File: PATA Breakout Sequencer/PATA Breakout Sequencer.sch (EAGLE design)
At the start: 11 parts

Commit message: some board layout
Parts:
- removed V10, V9: 74595N, 74ttl-din:74595N
- added IC1, IC2, IC3, IC4, IC5: 74HC165N, 74xx-eu:74HC165N
- added R1, R10, R11, R12, R13, R14, R15, R16, R17, R18, R19, R2, R20, R21, R22, R23, R24, R25, R26, R27, R28, R29, R3, R30, R31, R32, R33, R34, R35, R36, R37, R38, R39, R4, R40, R5, R6, R7, R8, R9: (no value), rcl:R-US_0204/5
- added SV2: (no value), con-lsta:FE20-2
- added SV3: (no value), con-lsta:FE15-2
- added SV5: (no value), con-lsta:FE18-2
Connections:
- new net A0: IC1A.A, R8.1, SV3.1, SV3.30
- new net A1: IC2A.A, R16.1
- new net A10: V61.QA
- new net A11: V71.QA
- new net A12: V81.QA
- new net A2: IC3A.A, R24.1
- new net A3: IC4A.A, R32.1
- new net A4: IC5A.A, R40.1
- new net A5: V11.QA
- new net A6: V21.QA
- new net A7: V31.QA
- new net A8: V41.QA
- new net A9: V51.QA
- new net B0: IC1A.B, R7.1, SV3.3
- new net B1: IC2A.B, R15.1
- new net B10: V61.QB
- new net B11: V71.QB
- new net B12: V81.QB
- new net B2: IC3A.B, R23.1
- new net B3: IC4A.B, R31.1
- new net B4: IC5A.B, R39.1
- new net B5: V11.QB
- new net B6: V21.QB
- new net B7: V31.QB
- new net B8: V41.QB
- new net B9: V51.QB
- new net C0: IC1A.C, R6.1, SV3.5
- new net C1: IC2A.C, R14.1
- new net C10: V61.QC
- new net C11: V71.QC
- new net C12: V81.QC
- new net C2: IC3A.C, R22.1
- new net C3: IC4A.C, R30.1
- new net C4: IC5A.C, R38.1
- new net C5: V11.QC
- new net C6: V21.QC
- new net C7: V31.QC
- new net C8: V41.QC
- new net C9: V51.QC
- new net D0: IC1A.D, R5.1, SV3.7
- new net D1: IC2A.D, R13.1
- new net D10: V61.QD
- new net D11: V71.QD
- new net D12: V81.QD
- new net D2: IC3A.D, R21.1
- new net D3: IC4A.D, R29.1
- new net D4: IC5A.D, R37.1
- new net D5: V11.QD
- new net D6: V21.QD
- new net D7: V31.QD
- new net D8: V41.QD
- new net D9: V51.QD
- new net E0: IC1A.E, R4.1, SV3.9
- new net E1: IC2A.E, R12.1
- new net E10: V61.QE
- new net E11: V71.QE
- new net E12: V81.QE
- new net E2: IC3A.E, R20.1
- new net E3: IC4A.E, R28.1
- new net E4: IC5A.E, R36.1
- new net E5: V11.QE
- new net E6: V21.QE
- new net E7: V31.QE
- new net E8: V41.QE
- new net E9: V51.QE
- new net F0: IC1A.F, R3.1, SV3.11
- new net F1: IC2A.F, R11.1
- new net F10: V61.QF
- new net F11: V71.QF
- new net F12: V81.QF
- new net F2: IC3A.F, R19.1
- new net F3: IC4A.F, R27.1
- new net F4: IC5A.F, R35.1
- new net F5: V11.QF
- new net F6: V21.QF
- new net F7: V31.QF
- new net F8: V41.QF
- new net F9: V51.QF
- new net G0: IC1A.G, R2.1, SV3.13
- new net G1: IC2A.G, R10.1
- new net G10: V61.QG
- new net G11: V71.QG
- new net G12: V81.QG
- new net G2: IC3A.G, R18.1
- new net G3: IC4A.G, R26.1
- new net G4: IC5A.G, R34.1
- new net G5: V11.QG
- new net G6: V21.QG
- new net G7: V31.QG
- new net G8: V41.QG
- new net G9: V51.QG
- new net H0: IC1A.H, R1.1, SV3.15
- new net H1: IC2A.H, R9.1
- new net H10: V61.QH
- new net H11: V71.QH
- new net H12: V81.QH
- new net H2: IC3A.H, R17.1
- new net H3: IC4A.H, R25.1
- new net H4: IC5A.H, R33.1
- new net H5: V11.QH
- new net H6: V21.QH
- new net H7: V31.QH
- new net H8: V41.QH
- new net H9: V51.QH
- new net N$10: SV3.16
- new net N$11: SV3.14
- new net N$12: SV3.12
- new net N$13: SV3.10
- new net N$14: SV3.8
- new net N$15: SV3.6
- new net N$16: SV3.4
- new net N$17: SV3.2
- new net N$21: SV3.29
- new net N$22: SV3.27
- new net N$23: SV3.25
- new net N$24: SV3.23
- new net N$25: SV3.21
- new net N$26: SV3.19
- new net N$27: SV3.17
- new net N$4: SV3.28
- new net N$5: SV3.26
- new net N$6: SV3.24
- new net N$7: SV3.22
- new net N$8: SV3.20
- new net N$9: SV3.18
- new net OUT0: V11.QH*, V21.SER
- new net OUT1: IC1A.SER, IC2A.QH, V21.QH*, V31.SER
- new net OUT2: IC2A.SER, IC3A.QH, V31.QH*, V41.SER
- new net OUT3: IC3A.SER, IC4A.QH, V41.QH*, V51.SER
- new net OUT4: IC4A.SER, IC5A.QH, V51.QH*, V61.SER
- new net OUT5: V61.QH*, V71.SER
- new net OUT6: V71.QH*, V81.SER
- new net OUT7: V81.QH*
- net +5V: now also R1.2, R10.2, R11.2, R12.2, R13.2, R14.2, R15.2, R16.2, R17.2, R18.2, R19.2, R2.2, R20.2, R21.2, R22.2, R23.2, R24.2, R25.2, R26.2, R27.2, R28.2, R29.2, R3.2, R30.2, R31.2, R32.2, R33.2, R34.2, R35.2, R36.2, R37.2, R38.2, R39.2, R4.2, R40.2, R5.2, R6.2, R7.2, R8.2, R9.2
- net DGND: now also IC1A.INH, IC2A.INH, IC3A.INH, IC4A.INH, IC5A.INH, IC5A.SER, V11.!G, V21.!G, V31.!G, V41.!G, V51.!G, V61.!G, V71.!G, V81.!G
- net LATCH_IN: now also IC1A.SH/!LD, IC2A.SH/!LD, IC3A.SH/!LD, IC4A.SH/!LD, IC5A.SH/!LD
- net LATCH_OUT: now also V11.RCK, V21.RCK, V31.RCK, V41.RCK, V51.RCK, V61.RCK, V71.RCK, V81.RCK
- net SERIAL_IN: now also IC1A.QH
- net SERIAL_OUT: now also V11.SER
- net SHIFT_IN: now also IC1A.CLK, IC2A.CLK, IC3A.CLK, IC4A.CLK, IC5A.CLK
- net SHIFT_OUT: now also V11.SRCK, V21.SRCK, V31.SRCK, V41.SRCK, V51.SRCK, V61.SRCK, V71.SRCK, V81.SRCK
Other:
- note added: "DATA FLOW"
- moved on the sheet: V1, V2, V3, V4, V5, V6, V7, V8

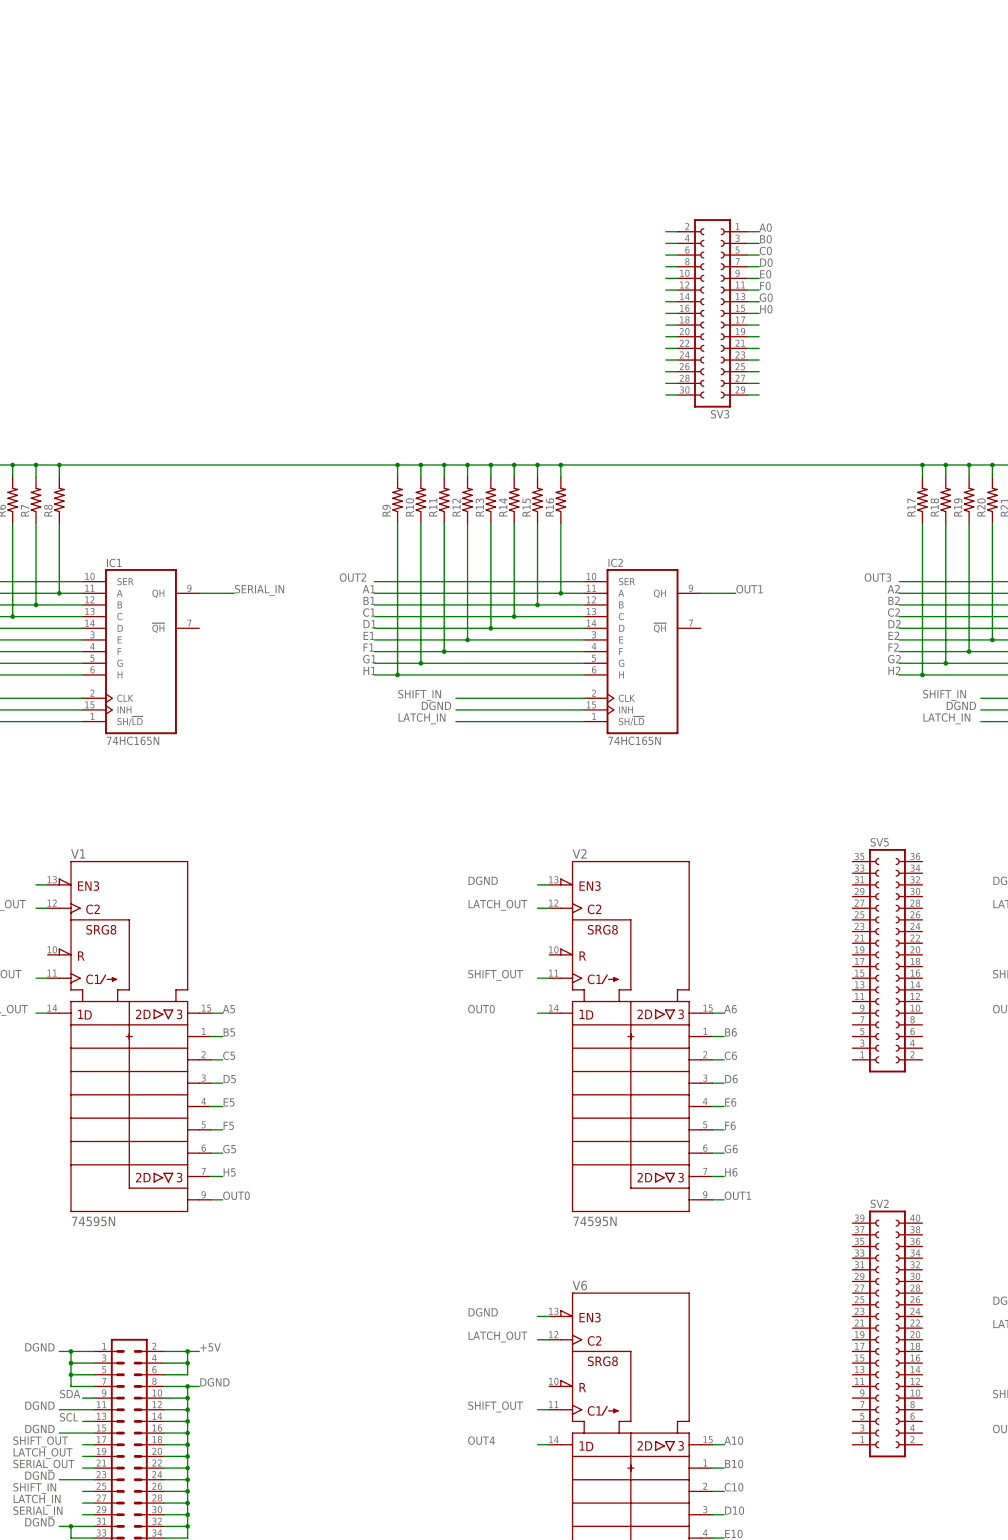
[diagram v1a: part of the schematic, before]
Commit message: split board into 2
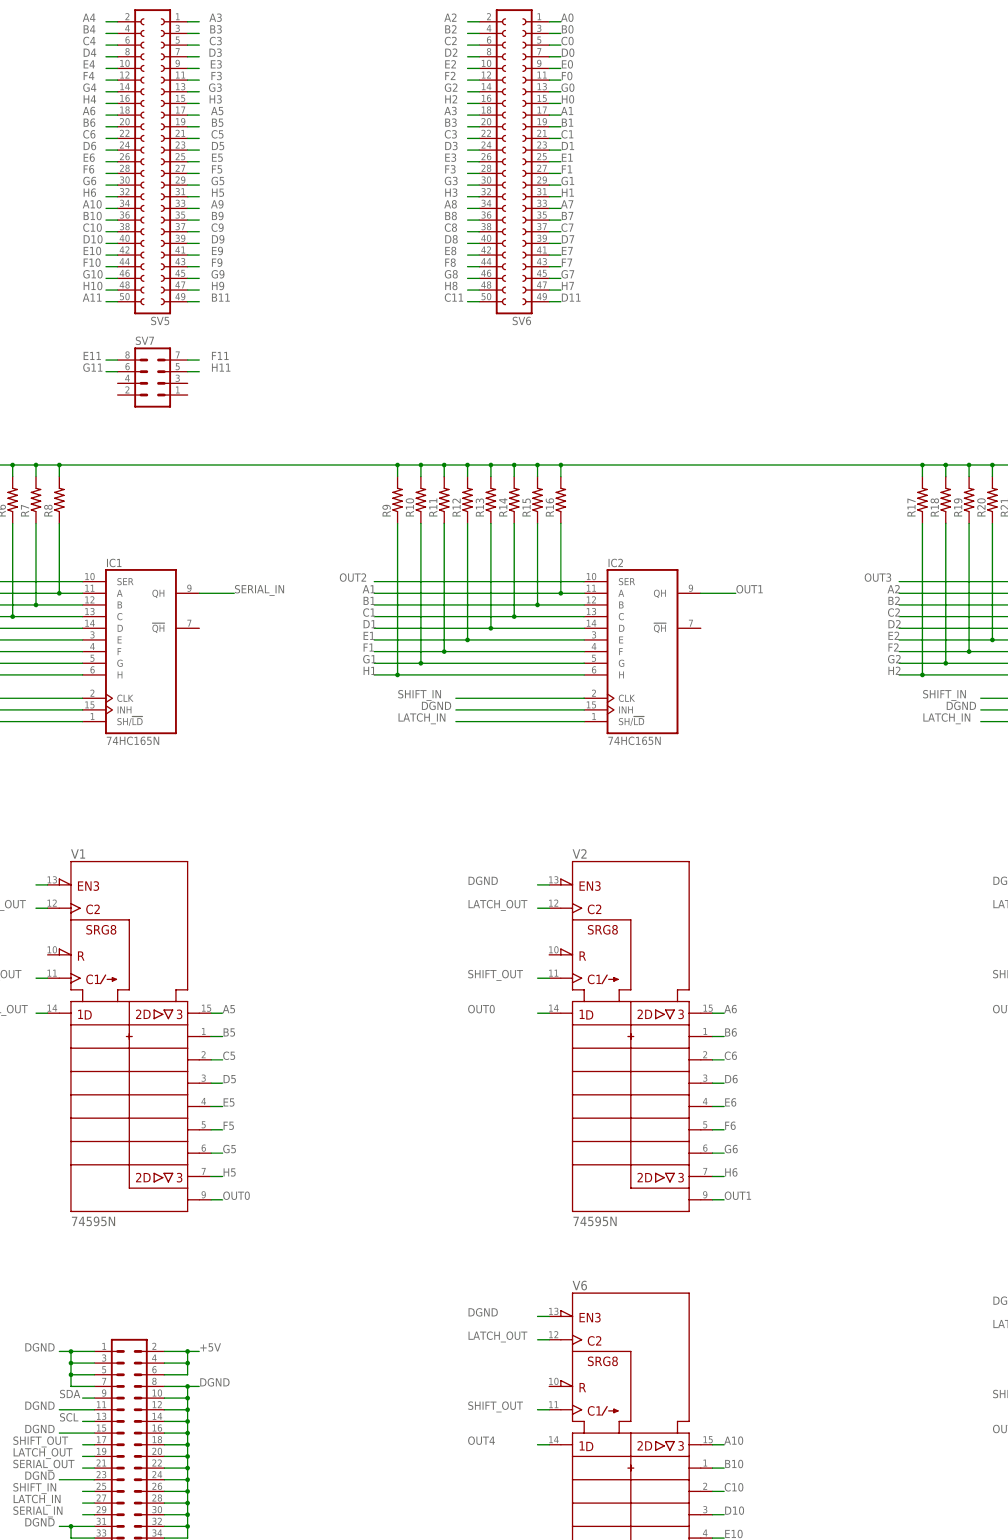
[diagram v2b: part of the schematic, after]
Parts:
- removed SV2: (no value), con-lsta:FE20-2
- removed SV3: (no value), con-lsta:FE15-2
- added SV6: (no value), con-lsta:FE25-2
- added SV7: (no value), con-lstb:MA04-2
- SV5: device con-lsta:FE18-2 -> con-lsta:FE25-2
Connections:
- removed net N$10: SV3.16
- removed net N$11: SV3.14
- removed net N$12: SV3.12
- removed net N$13: SV3.10
- removed net N$14: SV3.8
- removed net N$15: SV3.6
- removed net N$16: SV3.4
- removed net N$17: SV3.2
- removed net N$21: SV3.29
- removed net N$22: SV3.27
- removed net N$23: SV3.25
- removed net N$24: SV3.23
- removed net N$25: SV3.21
- removed net N$26: SV3.19
- removed net N$27: SV3.17
- removed net N$4: SV3.28
- removed net N$5: SV3.26
- removed net N$6: SV3.24
- removed net N$7: SV3.22
- removed net N$8: SV3.20
- removed net N$9: SV3.18
- net A0: now also SV6.1; no longer SV3.1, SV3.30
- net A1: now also SV6.17
- net A10: now also SV5.34
- net A11: now also SV5.50
- net A2: now also SV6.2
- net A3: now also SV5.1, SV6.18
- net A4: now also SV5.2
- net A5: now also SV5.17
- net A6: now also SV5.18
- net A7: now also SV6.33
- net A8: now also SV6.34
- net A9: now also SV5.33
- net B0: now also SV6.3; no longer SV3.3
- net B1: now also SV6.19
- net B10: now also SV5.36
- net B11: now also SV5.49
- net B2: now also SV6.4
- net B3: now also SV5.3, SV6.20
- net B4: now also SV5.4
- net B5: now also SV5.19
- net B6: now also SV5.20
- net B7: now also SV6.35
- net B8: now also SV6.36
- net B9: now also SV5.35
- net C0: now also SV6.5; no longer SV3.5
- net C1: now also SV6.21
- net C10: now also SV5.38
- net C11: now also SV6.50
- net C2: now also SV6.6
- net C3: now also SV5.5, SV6.22
- net C4: now also SV5.6
- net C5: now also SV5.21
- net C6: now also SV5.22
- net C7: now also SV6.37
- net C8: now also SV6.38
- net C9: now also SV5.37
- net D0: now also SV6.7; no longer SV3.7
- net D1: now also SV6.23
- net D10: now also SV5.40
- net D11: now also SV6.49
- net D2: now also SV6.8
- net D3: now also SV5.7, SV6.24
- net D4: now also SV5.8
- net D5: now also SV5.23
- net D6: now also SV5.24
- net D7: now also SV6.39
- net D8: now also SV6.40
- net D9: now also SV5.39
- net E0: now also SV6.9; no longer SV3.9
- net E1: now also SV6.25
- net E10: now also SV5.42
- net E11: now also SV7.8
- net E2: now also SV6.10
- net E3: now also SV5.9, SV6.26
- net E4: now also SV5.10
- net E5: now also SV5.25
- net E6: now also SV5.26
- net E7: now also SV6.41
- net E8: now also SV6.42
- net E9: now also SV5.41
- net F0: now also SV6.11; no longer SV3.11
- net F1: now also SV6.27
- net F10: now also SV5.44
- net F11: now also SV7.7
- net F2: now also SV6.12
- net F3: now also SV5.11, SV6.28
- net F4: now also SV5.12
- net F5: now also SV5.27
- net F6: now also SV5.28
- net F7: now also SV6.43
- net F8: now also SV6.44
- net F9: now also SV5.43
- net G0: now also SV6.13; no longer SV3.13
- net G1: now also SV6.29
- net G10: now also SV5.46
- net G11: now also SV7.6
- net G2: now also SV6.14
- net G3: now also SV5.13, SV6.30
- net G4: now also SV5.14
- net G5: now also SV5.29
- net G6: now also SV5.30
- net G7: now also SV6.45
- net G8: now also SV6.46
- net G9: now also SV5.45
- net H0: now also SV6.15; no longer SV3.15
- net H1: now also SV6.31
- net H10: now also SV5.48
- net H11: now also SV7.5
- net H2: now also SV6.16
- net H3: now also SV5.15, SV6.32
- net H4: now also SV5.16
- net H5: now also SV5.31
- net H6: now also SV5.32
- net H7: now also SV6.47
- net H8: now also SV6.48
- net H9: now also SV5.47

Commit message: Finished top board - ran DRC
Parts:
- removed IC1, IC2, IC3, IC4, IC5: 74HC165N, 74xx-eu:74HC165N
- removed R1, R10, R11, R12, R13, R14, R15, R16, R17, R18, R19, R2, R20, R21, R22, R23, R24, R25, R26, R27, R28, R29, R3, R30, R31, R32, R33, R34, R35, R36, R37, R38, R39, R4, R40, R5, R6, R7, R8, R9: (no value), rcl:R-US_0204/5
- removed SV5, SV6: (no value), con-lsta:FE25-2
- removed SV7: (no value), con-lstb:MA04-2
- added C1, C2, C3, C4, C5, C6, C7, C8: 4.7uF, rcl:C-EU050-024X044
- added JP1, JP2, JP3, JP4: (no value), pinhead:PINHD-1X16
- added JP6, JP7, JP8, JP9: (no value), pinhead:PINHD-2X4
- added SV3: (no value), con-lstb:MA05-2
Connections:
- removed net +5V: R1.2, R10.2, R11.2, R12.2, R13.2, R14.2, R15.2, R16.2, R17.2, R18.2, R19.2, R2.2, R20.2, R21.2, R22.2, R23.2, R24.2, R25.2, R26.2, R27.2, R28.2, R29.2, R3.2, R30.2, R31.2, R32.2, R33.2, R34.2, R35.2, R36.2, R37.2, R38.2, R39.2, R4.2, R40.2, R5.2, R6.2, R7.2, R8.2, R9.2, SV1.2, SV1.4, SV1.6
- removed net A0: IC1A.A, R8.1, SV6.1
- removed net A1: IC2A.A, R16.1, SV6.17
- removed net A2: IC3A.A, R24.1, SV6.2
- removed net A3: IC4A.A, R32.1, SV5.1, SV6.18
- removed net A4: IC5A.A, R40.1, SV5.2
- removed net B0: IC1A.B, R7.1, SV6.3
- removed net B1: IC2A.B, R15.1, SV6.19
- removed net B2: IC3A.B, R23.1, SV6.4
- removed net B3: IC4A.B, R31.1, SV5.3, SV6.20
- removed net B4: IC5A.B, R39.1, SV5.4
- removed net C0: IC1A.C, R6.1, SV6.5
- removed net C1: IC2A.C, R14.1, SV6.21
- removed net C2: IC3A.C, R22.1, SV6.6
- removed net C3: IC4A.C, R30.1, SV5.5, SV6.22
- removed net C4: IC5A.C, R38.1, SV5.6
- removed net D0: IC1A.D, R5.1, SV6.7
- removed net D1: IC2A.D, R13.1, SV6.23
- removed net D2: IC3A.D, R21.1, SV6.8
- removed net D3: IC4A.D, R29.1, SV5.7, SV6.24
- removed net D4: IC5A.D, R37.1, SV5.8
- removed net DGND: IC1A.INH, IC2A.INH, IC3A.INH, IC4A.INH, IC5A.INH, IC5A.SER, SV1.1, SV1.10, SV1.11, SV1.12, SV1.14, SV1.15, SV1.16, SV1.18, SV1.20, SV1.22, SV1.23, SV1.24, SV1.26, SV1.28, SV1.3, SV1.30, SV1.31, SV1.32, SV1.33, SV1.34, SV1.5, SV1.7, SV1.8, V11.!G, V21.!G, V31.!G, V41.!G, V51.!G, V61.!G, V71.!G, V81.!G
- removed net E0: IC1A.E, R4.1, SV6.9
- removed net E1: IC2A.E, R12.1, SV6.25
- removed net E2: IC3A.E, R20.1, SV6.10
- removed net E3: IC4A.E, R28.1, SV5.9, SV6.26
- removed net E4: IC5A.E, R36.1, SV5.10
- removed net F0: IC1A.F, R3.1, SV6.11
- removed net F1: IC2A.F, R11.1, SV6.27
- removed net F2: IC3A.F, R19.1, SV6.12
- removed net F3: IC4A.F, R27.1, SV5.11, SV6.28
- removed net F4: IC5A.F, R35.1, SV5.12
- removed net G0: IC1A.G, R2.1, SV6.13
- removed net G1: IC2A.G, R10.1, SV6.29
- removed net G2: IC3A.G, R18.1, SV6.14
- removed net G3: IC4A.G, R26.1, SV5.13, SV6.30
- removed net G4: IC5A.G, R34.1, SV5.14
- removed net H0: IC1A.H, R1.1, SV6.15
- removed net H1: IC2A.H, R9.1, SV6.31
- removed net H2: IC3A.H, R17.1, SV6.16
- removed net H3: IC4A.H, R25.1, SV5.15, SV6.32
- removed net H4: IC5A.H, R33.1, SV5.16
- new net +UB: C1.1, C2.1, C3.1, C4.1, C5.1, C6.1, C7.1, C8.1, JP6.1, JP6.3, JP6.5, JP6.7, JP7.1, JP7.3, JP7.5, JP7.7, JP8.1, JP8.3, JP8.5, JP8.7, JP9.1, JP9.3, JP9.5, JP9.7, SV1.2, SV1.4, SV1.6, SV3.2, SV3.9
- new net -UB: C1.2, C2.2, C3.2, C4.2, C5.2, C6.2, C7.2, C8.2, JP6.2, JP6.4, JP6.6, JP6.8, JP7.2, JP7.4, JP7.6, JP7.8, JP8.2, JP8.4, JP8.6, JP8.8, JP9.2, JP9.4, JP9.6, JP9.8, SV1.1, SV1.10, SV1.11, SV1.12, SV1.14, SV1.15, SV1.16, SV1.18, SV1.20, SV1.22, SV1.23, SV1.24, SV1.26, SV1.28, SV1.3, SV1.30, SV1.31, SV1.32, SV1.33, SV1.34, SV1.5, SV1.7, SV1.8, SV3.1, SV3.10, V11.!G, V21.!G, V31.!G, V41.!G, V51.!G, V61.!G, V71.!G, V81.!G
- net A10: now also JP3.8; no longer SV5.34
- net A11: now also JP2.8; no longer SV5.50
- net A12: now also JP1.8
- net A5: now also JP1.16; no longer SV5.17
- net A6: now also JP2.16; no longer SV5.18
- net A7: now also JP3.16; no longer SV6.33
- net A8: now also JP4.16; no longer SV6.34
- net A9: now also JP4.8; no longer SV5.33
- net B10: now also JP3.7; no longer SV5.36
- net B11: now also JP2.7; no longer SV5.49
- net B12: now also JP1.7
- net B5: now also JP1.15; no longer SV5.19
- net B6: now also JP2.15; no longer SV5.20
- net B7: now also JP3.15; no longer SV6.35
- net B8: now also JP4.15; no longer SV6.36
- net B9: now also JP4.7; no longer SV5.35
- net C10: now also JP3.6; no longer SV5.38
- net C11: now also JP2.6; no longer SV6.50
- net C12: now also JP1.6
- net C5: now also JP1.14; no longer SV5.21
- net C6: now also JP2.14; no longer SV5.22
- net C7: now also JP3.14; no longer SV6.37
- net C8: now also JP4.14; no longer SV6.38
- net C9: now also JP4.6; no longer SV5.37
- net D10: now also JP3.5; no longer SV5.40
- net D11: now also JP2.5; no longer SV6.49
- net D12: now also JP1.5
- net D5: now also JP1.13; no longer SV5.23
- net D6: now also JP2.13; no longer SV5.24
- net D7: now also JP3.13; no longer SV6.39
- net D8: now also JP4.13; no longer SV6.40
- net D9: now also JP4.5; no longer SV5.39
- net E10: now also JP3.4; no longer SV5.42
- net E11: now also JP2.4; no longer SV7.8
- net E12: now also JP1.4
- net E5: now also JP1.12; no longer SV5.25
- net E6: now also JP2.12; no longer SV5.26
- net E7: now also JP3.12; no longer SV6.41
- net E8: now also JP4.12; no longer SV6.42
- net E9: now also JP4.4; no longer SV5.41
- net F10: now also JP3.3; no longer SV5.44
- net F11: now also JP2.3; no longer SV7.7
- net F12: now also JP1.3
- net F5: now also JP1.11; no longer SV5.27
- net F6: now also JP2.11; no longer SV5.28
- net F7: now also JP3.11; no longer SV6.43
- net F8: now also JP4.11; no longer SV6.44
- net F9: now also JP4.3; no longer SV5.43
- net G10: now also JP3.2; no longer SV5.46
- net G11: now also JP2.2; no longer SV7.6
- net G12: now also JP1.2
- net G5: now also JP1.10; no longer SV5.29
- net G6: now also JP2.10; no longer SV5.30
- net G7: now also JP3.10; no longer SV6.45
- net G8: now also JP4.10; no longer SV6.46
- net G9: now also JP4.2; no longer SV5.45
- net H10: now also JP3.1; no longer SV5.48
- net H11: now also JP2.1; no longer SV7.5
- net H12: now also JP1.1
- net H5: now also JP1.9; no longer SV5.31
- net H6: now also JP2.9; no longer SV5.32
- net H7: now also JP3.9; no longer SV6.47
- net H8: now also JP4.9; no longer SV6.48
- net H9: now also JP4.1; no longer SV5.47
- net LATCH_IN: now also SV3.5, SV3.6; no longer IC1A.SH/!LD, IC2A.SH/!LD, IC3A.SH/!LD, IC4A.SH/!LD, IC5A.SH/!LD
- net OUT1: no longer IC1A.SER, IC2A.QH
- net OUT2: no longer IC2A.SER, IC3A.QH
- net OUT3: no longer IC3A.SER, IC4A.QH
- net OUT4: no longer IC4A.SER, IC5A.QH
- net SERIAL_IN: now also SV3.7, SV3.8; no longer IC1A.QH
- net SHIFT_IN: now also SV3.3, SV3.4; no longer IC1A.CLK, IC2A.CLK, IC3A.CLK, IC4A.CLK, IC5A.CLK
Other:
- moved on the sheet: V2, V3, V4, V5, V6, V7, V8
